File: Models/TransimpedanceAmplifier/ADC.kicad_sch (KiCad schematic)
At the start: 0 parts

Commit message: Filled in some detail
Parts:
- added U3: ADS8699IPW, PW16_TEX, symbol ADS8699:ADS8699IPW
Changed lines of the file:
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@@
 	(generator_version "9.0")
 	(paper "A4")
+	(symbol
+		(lib_id "ADS8699:ADS8699IPW")
+		(at 114.3 88.9 0)
+		(unit 1)
+		(exclude_from_sim no)
+		(in_bom yes)
+		(on_board yes)
+		(dnp no)
+		(fields_autoplaced yes)
+		(property "Reference" "U3"
+			(at 149.86 78.74 0)
+			(effects
+				(font
+					(size 1.524 1.524)
+				)
+			)
+		)
+		(property "Value" "ADS8699IPW"
+			(at 149.86 81.28 0)
+			(effects
+				(font
+					(size 1.524 1.524)
+				)
+			)
+		)
+		(property "Footprint" "PW16_TEX"
+			(at 114.3 88.9 0)
+			(effects
+				(font
+					(size 1.27 1.27)
+					(italic yes)
+				)
+				(hide yes)
+			)
+		)
+		(property "Datasheet" "https://www.ti.com/lit/gpn/ads8699"
+			(at 114.3 88.9 0)
+			(effects
+				(font
+					(size 1.27 1.27)
+					(italic yes)
+				)
+				(hide yes)
+			)
+		)
+		(property "Description" ""
+			(at 114.3 88.9 0)
+			(effects
+				(font
+					(size 1.27 1.27)
+				)
+				(hide yes)
+			)
+		)
+		(pin "1"
+		)
+		(pin "2"
+		)
+		(pin "3"
+		)
+		(pin "4"
+		)
+		(pin "5"
+		)
+		(pin "6"
+		)
+		(pin "7"
+		)
+		(pin "8"
+		)
+		(pin "16"
+		)
+		(pin "15"
+		)
+		(pin "14"
+		)
+		(pin "13"
+		)
+		(pin "12"
+		)
+		(pin "11"
+		)
+		(pin "10"
+		)
+		(pin "9"
+		)
+		(instances
+			(project ""
+				(path "/ec9f2ae3-e40d-40eb-9760-2b611ee8efd1/49c90445-9dec-4844-815f-c72a1415129d"
+					(reference "U3")
+					(unit 1)
+				)
+			)
+		)
+	)
 )

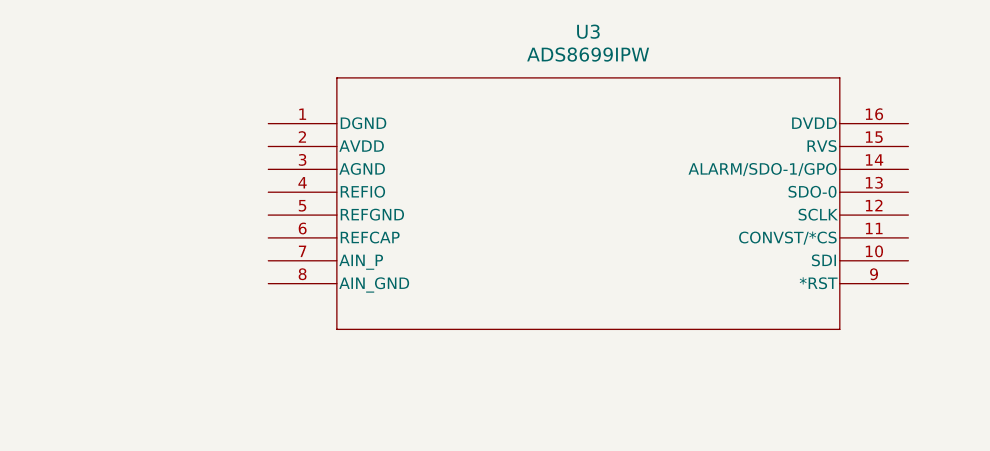
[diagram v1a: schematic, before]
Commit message: Specified the power I/O sheet pins for the ADC
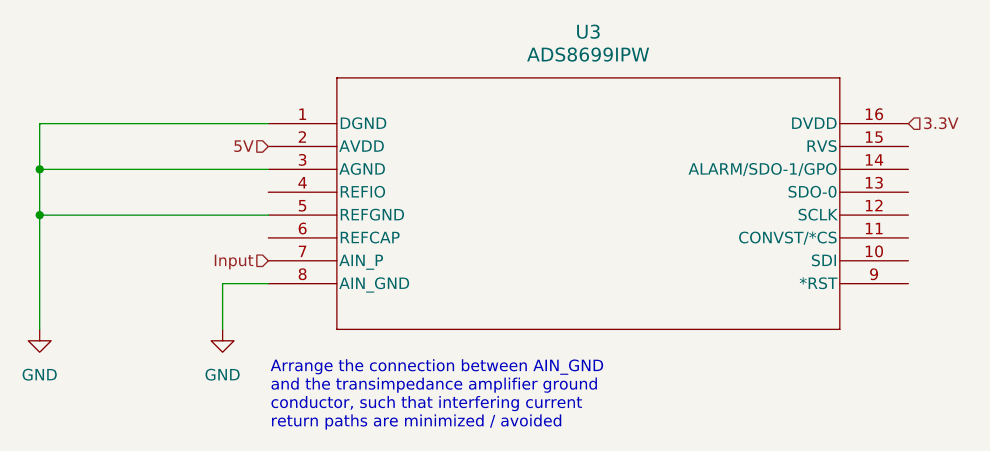
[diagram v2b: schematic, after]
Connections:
- net GND: now reaches U3.1 (DGND)
- net GND: now also U3.3 (AGND), U3.5 (REFGND), U3.8 (AIN_GND)
- net 3.3V: now reaches U3.16 (DVDD)
- net 5V: now reaches U3.2 (AVDD)
- net Input: now reaches U3.7 (AIN_P)
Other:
- note added: "Arrange the connection between AIN_GND and the transimpedance amplifier ground conductor, such that interfering current return paths are minimized / avoided"

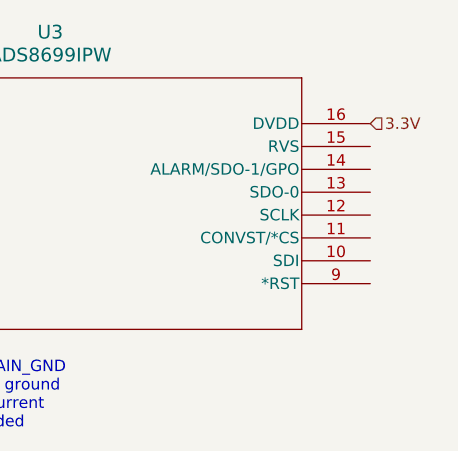
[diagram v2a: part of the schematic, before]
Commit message: Assigned all the SPI pins
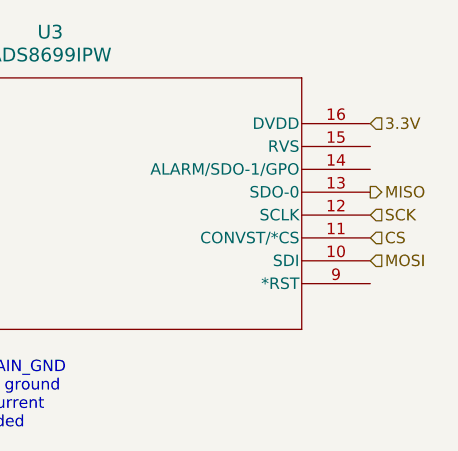
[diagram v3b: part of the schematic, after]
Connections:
- net MOSI: now reaches U3.10 (SDI)
- net CS: now reaches U3.11 (CONVST/*CS)
- net SCK: now reaches U3.12 (SCLK)
- net MISO: now reaches U3.13 (SDO-0)
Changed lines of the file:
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@@
+		)
+	)
+	(hierarchical_label "MOSI"
+		(shape input)
+		(at 185.42 104.14 0)
+		(effects
+			(font
+				(size 1.27 1.27)
+			)
+			(justify left)
 		)
 	)
@@
 		)
 	)
+	(hierarchical_label "CS"
+		(shape input)
+		(at 185.42 101.6 0)
+		(effects
+			(font
+				(size 1.27 1.27)
+			)
+			(justify left)
+		)
+	)
+	(hierarchical_label "MISO"
+		(shape output)
+		(at 185.42 96.52 0)
+		(effects
+			(font
+				(size 1.27 1.27)
+			)
+			(justify left)
+		)
+	)
+	(hierarchical_label "SCK"
+		(shape input)
+		(at 185.42 99.06 0)
+		(effects
+			(font
+				(size 1.27 1.27)
+			)
+			(justify left)
+		)
+	)

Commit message: All suppliers are out of stock of LM7915L in the simple TO-92-3 package. Resolve this by first tabulating the maximum possible current on each regulator.
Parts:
- U3: Purchase Link (none) -> https://www.digikey.com/en/products/detail/texas-instrument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
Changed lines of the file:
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@@
+			)
+		)
+		(property "Purchase Link" "https://www.digikey.com/en/products/detail/texas-instruments/ADS8699IPWR/6600065"
+			(at 114.3 88.9 0)
+			(effects
+				(font
+					(size 1.27 1.27)
+				)
+				(hide yes)
 			)
 		)

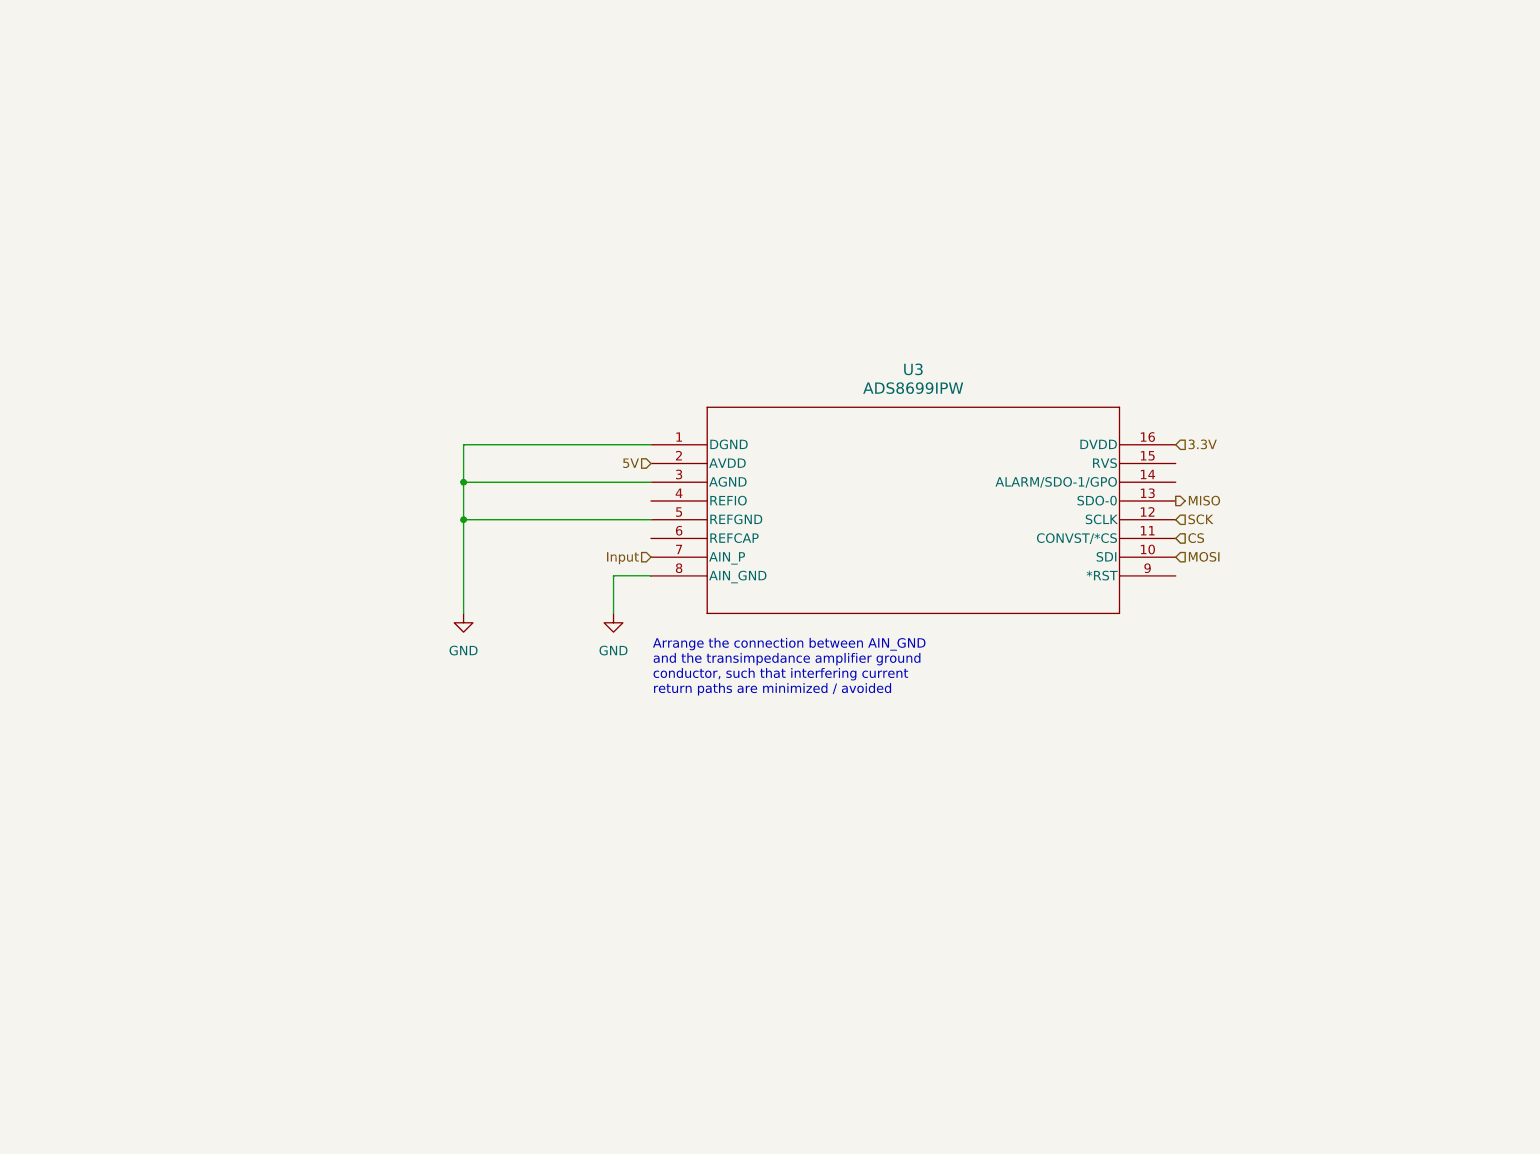
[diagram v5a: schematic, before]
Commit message: Finished writing the ADC's network
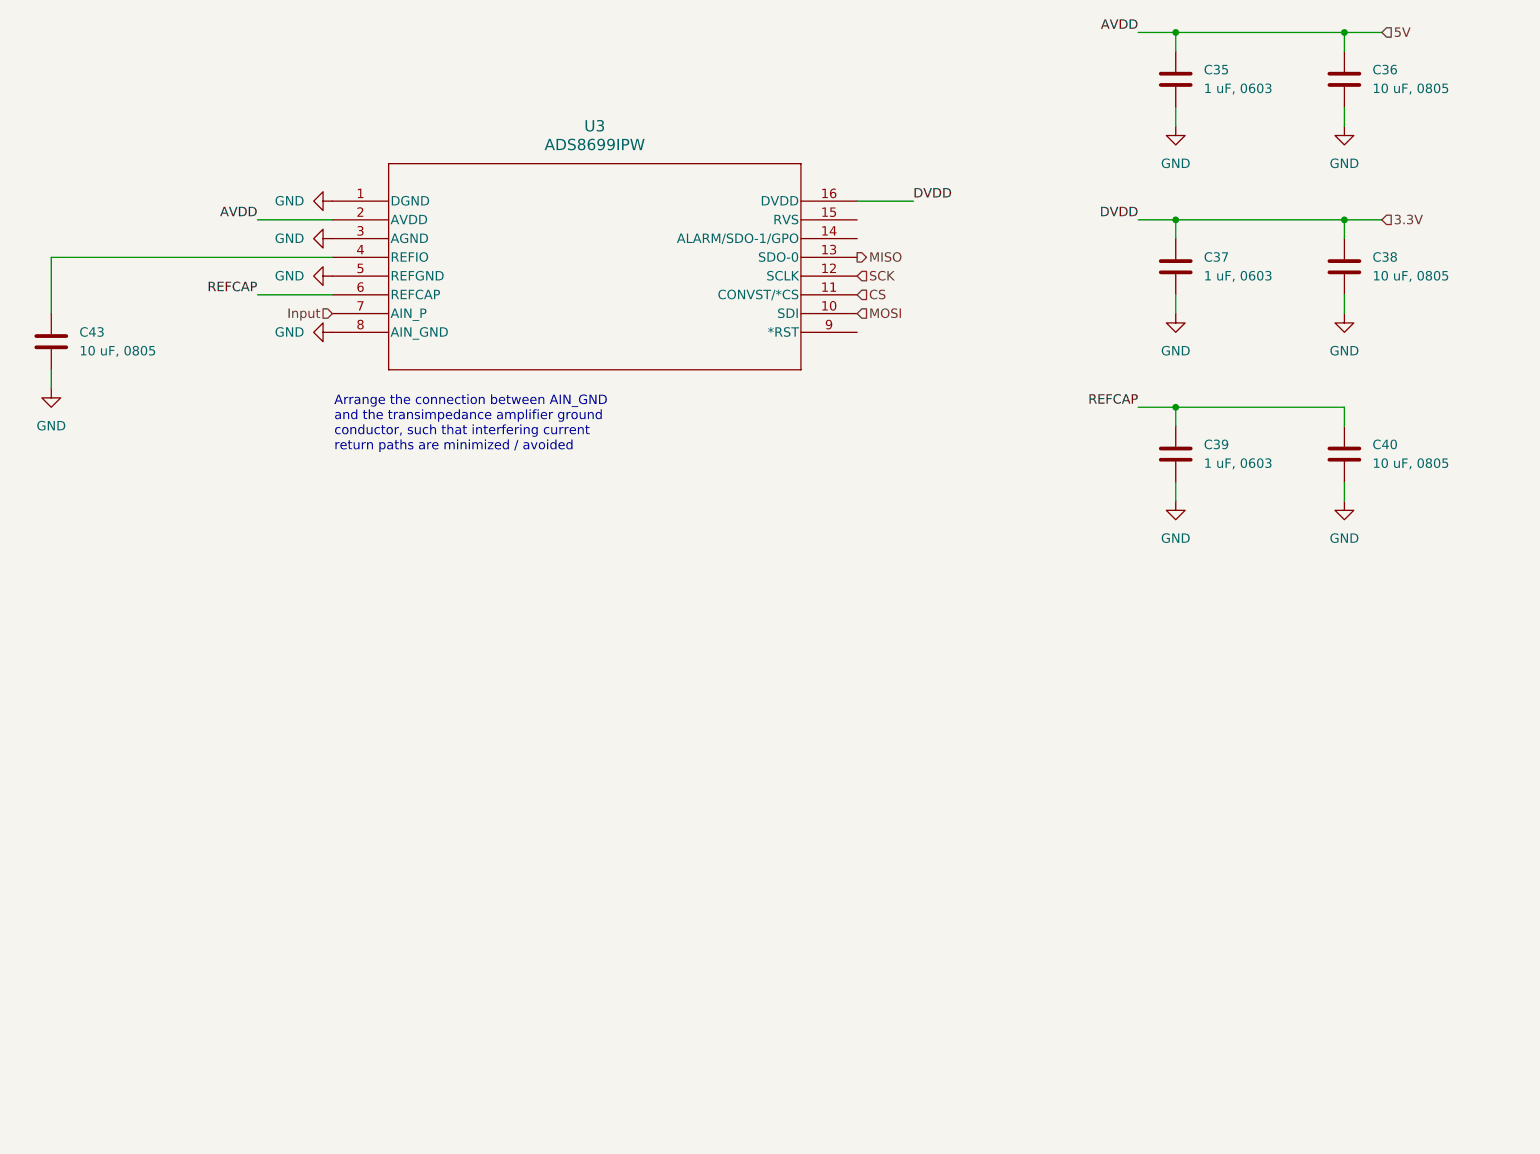
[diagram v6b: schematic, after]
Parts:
- added C35, C37, C39: 1 uF, 0603, symbol Device:C
- added C36, C38, C40, C43: 10 uF, 0805, symbol Device:C
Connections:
- net 3.3V: now also C37.1, C38.1
- net 5V: now also C35.1, C36.1
- net GND: now also C35.2, C36.2, C37.2, C38.2, C39.2, C40.2, C43.2
- net at U3.4 (REFIO): now also C43.1
- net REFCAP: now reaches U3.6 (REFCAP)
- net REFCAP: now also C39.1, C40.1
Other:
- moved on the sheet: U3

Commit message: Finished for today
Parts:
- C35, C36, C37, C38, C39, C40, C43: Purchase Link (none) -> https://www.digikey.com/en/products/detail/murata-electroni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
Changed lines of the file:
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@@
+			)
+		)
+		(property "Purchase Link" "https://www.digikey.com/en/products/detail/murata-electronics/GRT188R61H105KE13D/5416752"
+			(at 185.42 39.37 0)
+			(effects
+				(font
+					(size 1.27 1.27)
+				)
+				(hide yes)
 			)
 		)
@@
 			)
 		)
+		(property "Purchase Link" "https://www.digikey.com/en/products/detail/murata-electronics/GRT188R61H105KE13D/5416752"
+			(at 185.42 90.17 0)
+			(effects
+				(font
+					(size 1.27 1.27)
+				)
+				(hide yes)
+			)
+		)
 		(pin "1"
 		)
@@
 			)
 		)
-		(property "Purchase Link" ""
+		(property "Purchase Link" "https://www.digikey.com/en/products/detail/murata-electronics/GRM21BR61E106KA73K/4905532"
 			(at 208.28 64.77 0)
 			(effects
@@
 			)
 		)
+		(property "Purchase Link" "https://www.digikey.com/en/products/detail/murata-electronics/GRT188R61H105KE13D/5416752"
+			(at 185.42 64.77 0)
+			(effects
+				(font
+					(size 1.27 1.27)
+				)
+				(hide yes)
+			)
+		)
 		(pin "1"
 		)
@@
 			)
 		)
-		(property "Purchase Link" ""
+		(property "Purchase Link" "https://www.digikey.com/en/products/detail/murata-electronics/GRM21BR61E106KA73K/4905532"
 			(at 208.28 39.37 0)
 			(effects
@@
 			)
 		)
-		(property "Purchase Link" ""
+		(property "Purchase Link" "https://www.digikey.com/en/products/detail/murata-electronics/GRM21BR61E106KA73K/4905532"
 			(at 33.02 74.93 0)
 			(effects
@@
 			)
 		)
-		(property "Purchase Link" ""
+		(property "Purchase Link" "https://www.digikey.com/en/products/detail/murata-electronics/GRM21BR61E106KA73K/4905532"
 			(at 208.28 90.17 0)
 			(effects
